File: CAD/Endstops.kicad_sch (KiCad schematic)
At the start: 38 parts, among them Q21 MMBTA06-7-F, Q22 MMBTA06-7-F, U20 Optoisolator, U23 Optoisolator, U27 Optoisolator, U28 Optoisolator

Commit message: Part Alternatives
Changed some alternatives for certain parts as they are out of stock and some won't come in until March 27
Also changed C6 so it uses the same cap as C29 so that manufacturing costs are lower
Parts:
- R158, R160, R2, R4, R8: Part Number AC0402FR-0727KL -> AC0402FR-0727KL or AF0402FR-0727KL
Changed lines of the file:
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@@
 			)
 		)
-		(property "Part Number" "AC0402FR-0727KL"
+		(property "Part Number" "AC0402FR-0727KL or AF0402FR-0727KL"
 			(at 40.64 27.94 0)
 			(hide yes)
@@
 			)
 		)
-		(property "Part Number" "AC0402FR-0727KL"
+		(property "Part Number" "AC0402FR-0727KL or AF0402FR-0727KL"
 			(at 71.12 27.94 0)
 			(hide yes)
@@
 			)
 		)
-		(property "Part Number" "AC0402FR-0727KL"
+		(property "Part Number" "AC0402FR-0727KL or AF0402FR-0727KL"
 			(at 109.22 27.94 0)
 			(hide yes)
@@
 			)
 		)
-		(property "Part Number" "AC0402FR-0727KL"
+		(property "Part Number" "AC0402FR-0727KL or AF0402FR-0727KL"
 			(at 40.64 45.72 0)
 			(hide yes)
@@
 			)
 		)
-		(property "Part Number" "AC0402FR-0727KL"
+		(property "Part Number" "AC0402FR-0727KL or AF0402FR-0727KL"
 			(at 71.12 45.72 0)
 			(hide yes)

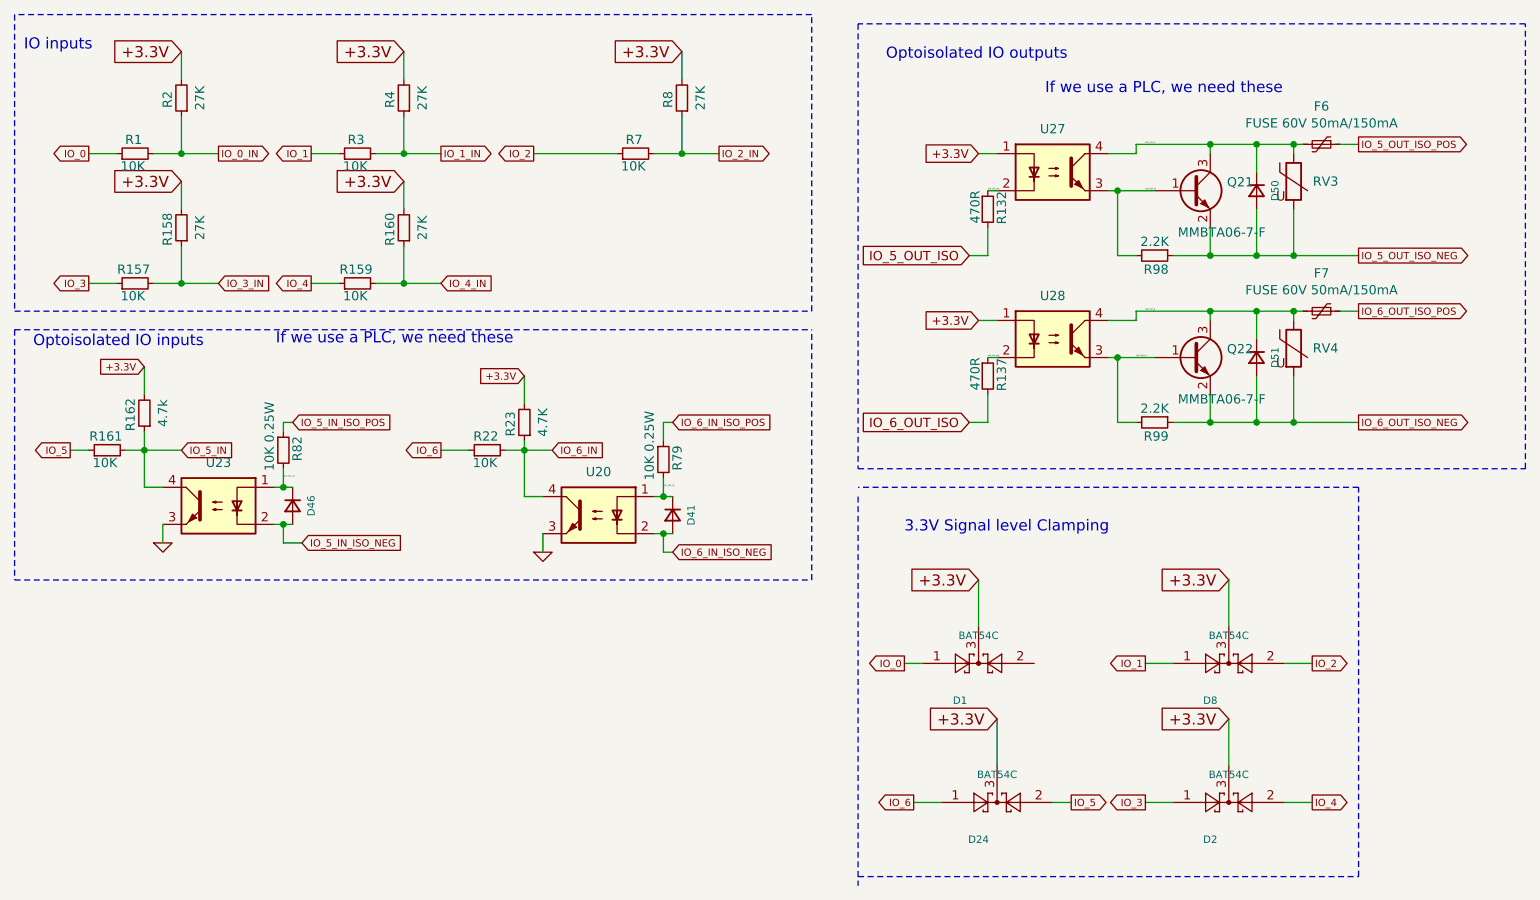
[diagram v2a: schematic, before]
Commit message: Readjust some misc traces + more DNP parts
Readjusted several traces for signal integrity
Made Optoisolators (the component itself, not the circuit) DNP
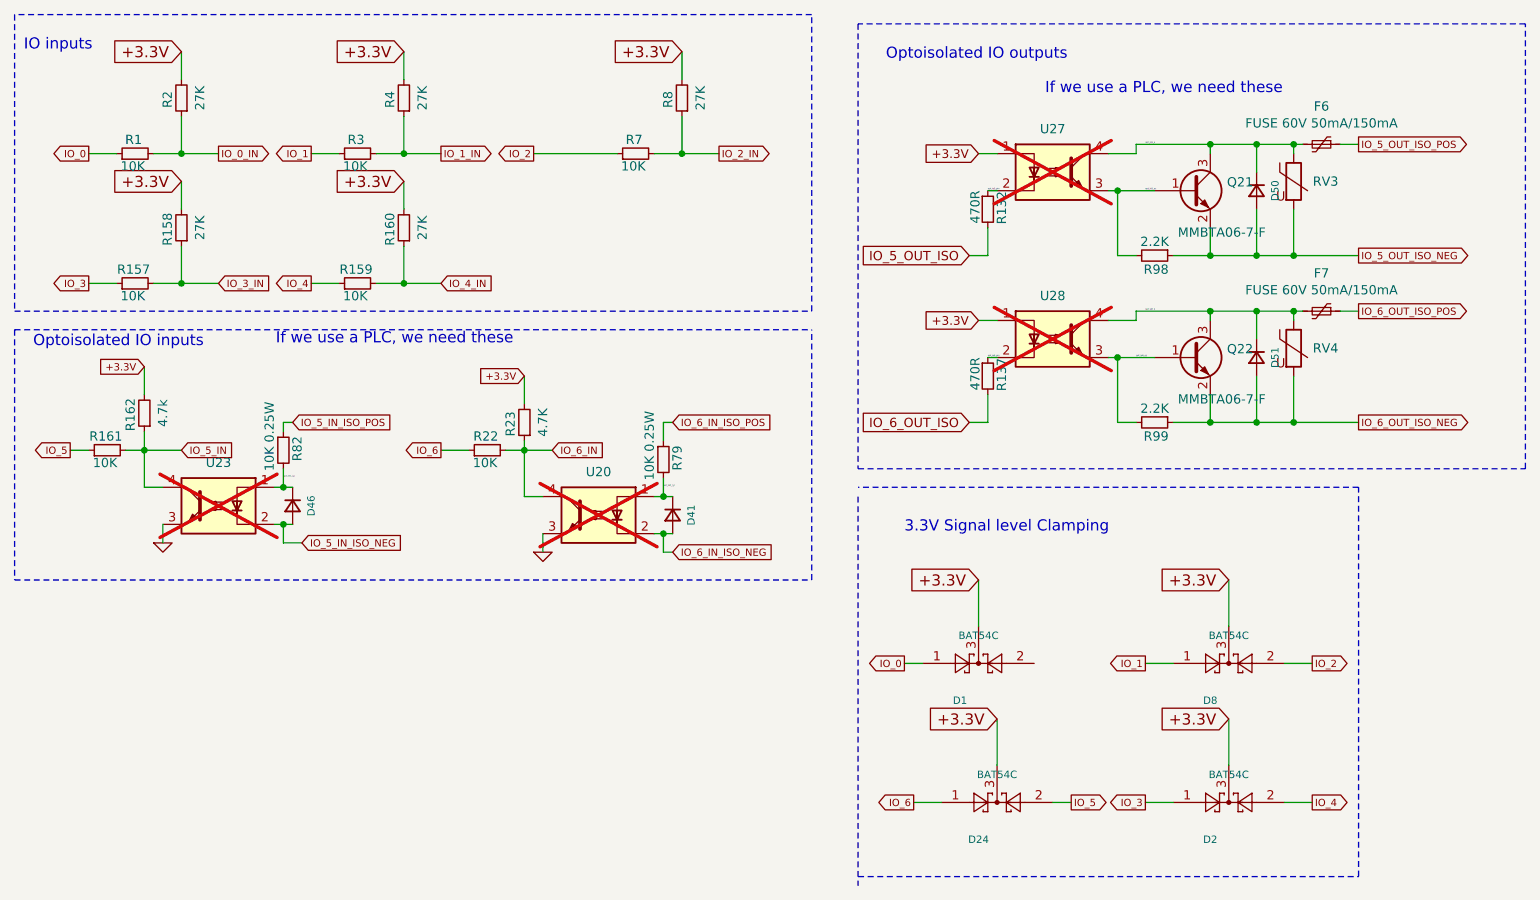
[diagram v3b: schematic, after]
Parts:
- U20, U23, U27, U28: now not fitted; now left out of the parts list
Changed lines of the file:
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@@
 		(body_style 1)
 		(exclude_from_sim no)
-		(in_bom yes)
+		(in_bom no)
 		(on_board yes)
 		(in_pos_files yes)
-		(dnp no)
+		(dnp yes)
 		(property "Reference" "U23"
 			(at 45.72 77.9018 0)
@@
 		(body_style 1)
 		(exclude_from_sim no)
-		(in_bom yes)
+		(in_bom no)
 		(on_board yes)
 		(in_pos_files yes)
-		(dnp no)
+		(dnp yes)
 		(property "Reference" "U20"
 			(at 97.79 79.1718 0)
@@
 		(body_style 1)
 		(exclude_from_sim no)
-		(in_bom yes)
+		(in_bom no)
 		(on_board yes)
 		(in_pos_files yes)
-		(dnp no)
+		(dnp yes)
 		(property "Reference" "U27"
 			(at 160.02 32.1818 0)
@@
 		(body_style 1)
 		(exclude_from_sim no)
-		(in_bom yes)
+		(in_bom no)
 		(on_board yes)
 		(in_pos_files yes)
-		(dnp no)
+		(dnp yes)
 		(property "Reference" "U28"
 			(at 160.02 55.0418 0)
